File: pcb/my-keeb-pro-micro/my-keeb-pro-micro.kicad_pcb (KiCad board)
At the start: 2 copper layers, 190.5 x 95.2 mm, 94 parts, among them SW1 SW_Push, U1 ProMicro

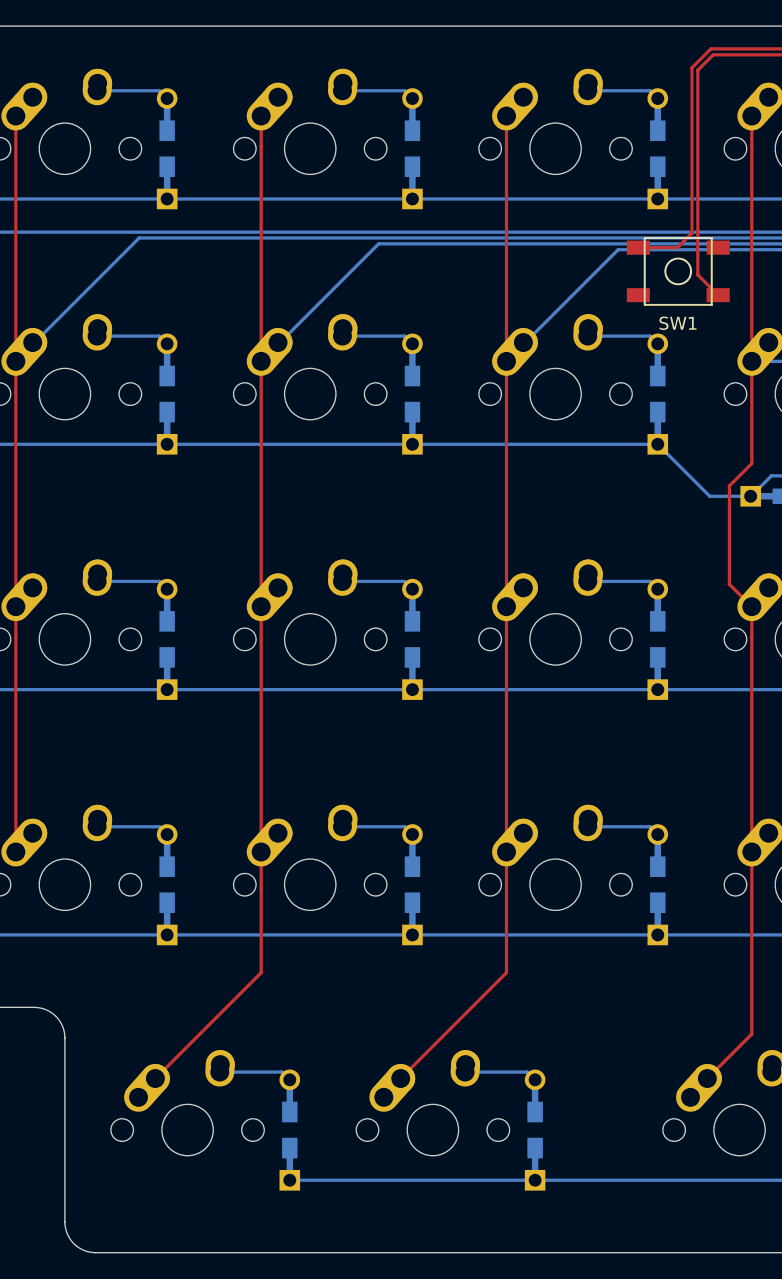
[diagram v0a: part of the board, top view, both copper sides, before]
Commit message: Added logo to pro micro model
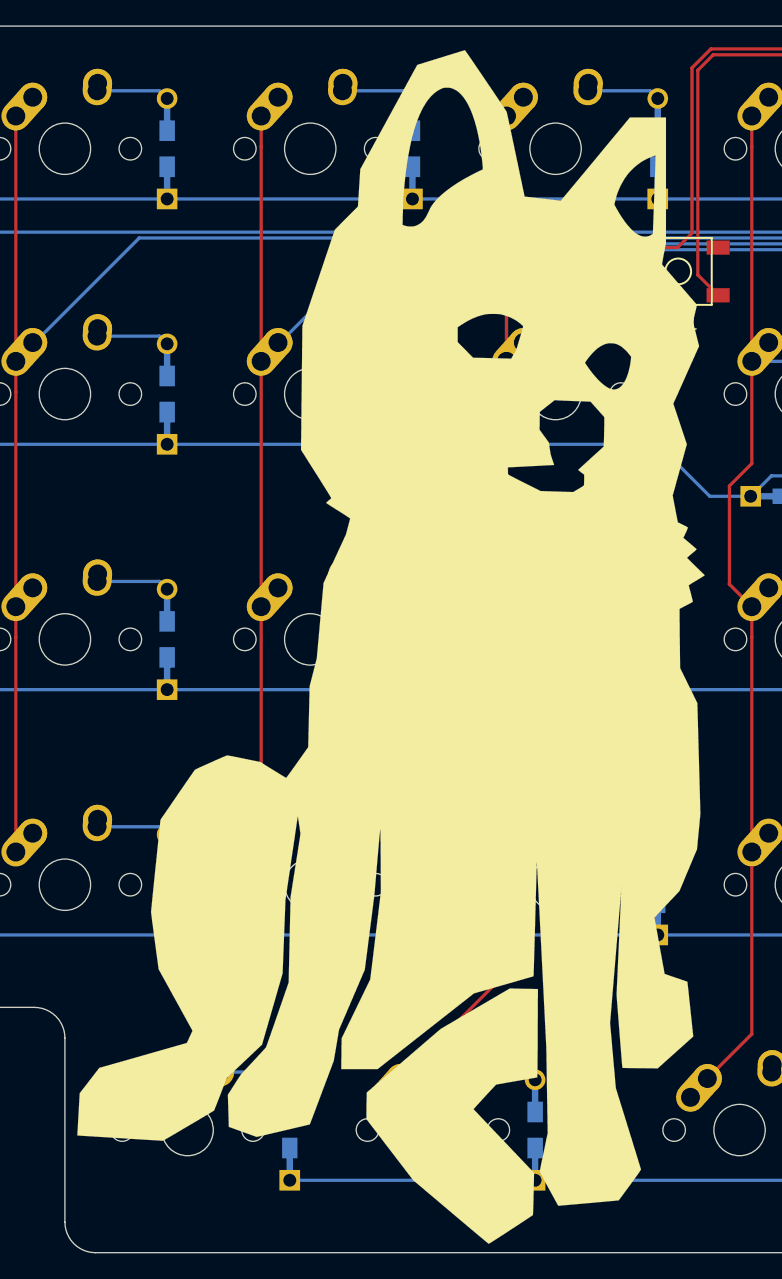
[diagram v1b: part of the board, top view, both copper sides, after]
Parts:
- added G***: LOGO, Sasha-sit:B.SilkS_g13524, B.Cu at (66.7, 51.6)
- added G***: LOGO, Sasha-sit:B.SilkS_g13524, F.Cu at (148.4, 50.8)
